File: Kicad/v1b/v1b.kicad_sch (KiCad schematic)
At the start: 11 parts, among them U1 65c02

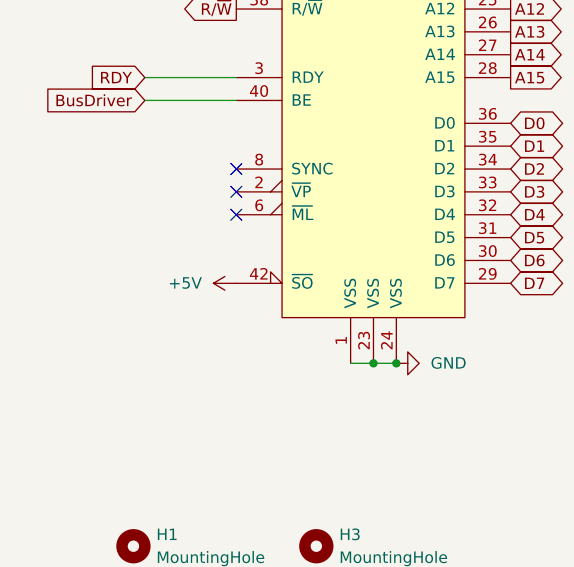
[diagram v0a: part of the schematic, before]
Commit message: Video ROM update, cart files, v1b main board
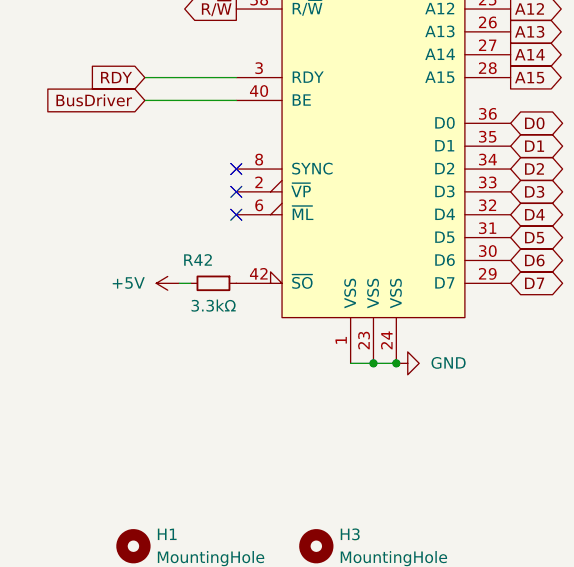
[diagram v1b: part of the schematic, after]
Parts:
- added R42: 3.3kΩ, Resistor_THT:R_Axial_DIN0204_L3.6mm_D1.6mm_P7.62mm_Horizontal, symbol Device:R_Small
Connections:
- net +5V: now also R42.2; no longer U1.42 (~{SO})
- new net: R42.1, U1.42 (~{SO})
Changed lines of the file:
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@@
+    (stroke (width 0) (type default))
+  )
+  (wire (pts (xy 29.21 85.09) (xy 30.48 85.09))
     (stroke (width 0) (type default))
   )
@@
     )
   )
+  (symbol (lib_id "power:+5V") (at 29.21 85.09 90) (unit 1)
+    (in_bom yes) (on_board yes) (dnp no) (fields_autoplaced)
+    (property "Reference" "#PWR01" (at 33.02 85.09 0)
+      (effects (font (size 1.27 1.27)) hide)
+    )
+    (property "Value" "+5V" (at 25.4 85.09 90)
+      (effects (font (size 1.27 1.27)) (justify left))
+    )
+    (property "Footprint" "" (at 29.21 85.09 0)
+      (effects (font (size 1.27 1.27)) hide)
+    )
+    (property "Datasheet" "" (at 29.21 85.09 0)
+      (effects (font (size 1.27 1.27)) hide)
+    )
+    (pin "1")
+    (instances
+      (project "v1b"
+        (path "/82bc3382-6295-4121-a2db-2433a00f189b"
+          (reference "#PWR01") (unit 1)
+        )
+      )
+    )
+  )
   (symbol (lib_id "Device:C") (at 87.63 66.04 0) (unit 1)
     (in_bom yes) (on_board yes) (dnp no) (fields_autoplaced)
@@
     )
   )
-  (symbol (lib_id "power:+5V") (at 35.56 85.09 90) (unit 1)
-    (in_bom yes) (on_board yes) (dnp no) (fields_autoplaced)
-    (property "Reference" "#PWR01" (at 39.37 85.09 0)
-      (effects (font (size 1.27 1.27)) hide)
-    )
-    (property "Value" "+5V" (at 31.75 85.09 90)
-      (effects (font (size 1.27 1.27)) (justify left))
-    )
-    (property "Footprint" "" (at 35.56 85.09 0)
-      (effects (font (size 1.27 1.27)) hide)
-    )
-    (property "Datasheet" "" (at 35.56 85.09 0)
-      (effects (font (size 1.27 1.27)) hide)
-    )
-    (pin "1")
-    (instances
-      (project "v1b"
-        (path "/82bc3382-6295-4121-a2db-2433a00f189b"
-          (reference "#PWR01") (unit 1)
-        )
-      )
+  (symbol (lib_id "Device:R_Small") (at 33.02 85.09 270) (unit 1)
+    (in_bom yes) (on_board yes) (dnp no)
+    (property "Reference" "R42" (at 33.02 82.55 90)
+      (effects (font (size 1.27 1.27)) (justify right))
+    )
+    (property "Value" "3.3kΩ" (at 35.56 87.63 90)
+      (effects (font (size 1.27 1.27)) (justify right))
+    )
+    (property "Footprint" "Resistor_THT:R_Axial_DIN0204_L3.6mm_D1.6mm_P7.62mm_Horizontal" (at 33.02 85.09 0)
+      (effects (font (size 1.27 1.27)) hide)
+    )
+    (property "Datasheet" "~" (at 33.02 85.09 0)
+      (effects (font (size 1.27 1.27)) hide)
+    )
+    (pin "1")
+    (pin "2")
+    (instances
+      (project "v1b"
+        (path "/82bc3382-6295-4121-a2db-2433a00f189b"
+          (reference "R42") (unit 1)
+        )
+      )
